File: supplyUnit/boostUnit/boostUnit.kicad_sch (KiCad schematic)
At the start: 22 parts, among them J1 Conn_02x03_Counter_Clockwise, J2 Conn_02x03_Counter_Clockwise

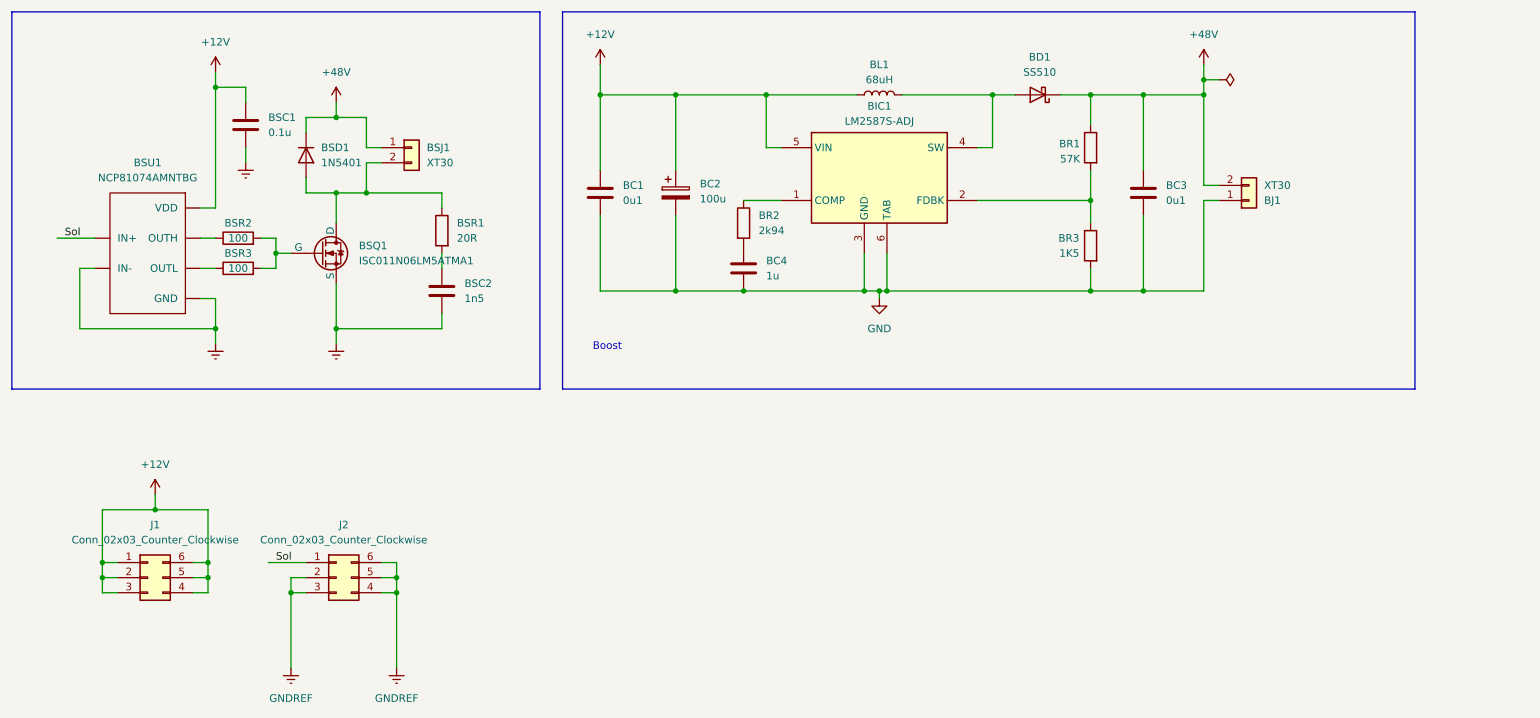
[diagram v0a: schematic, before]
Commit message: new boost
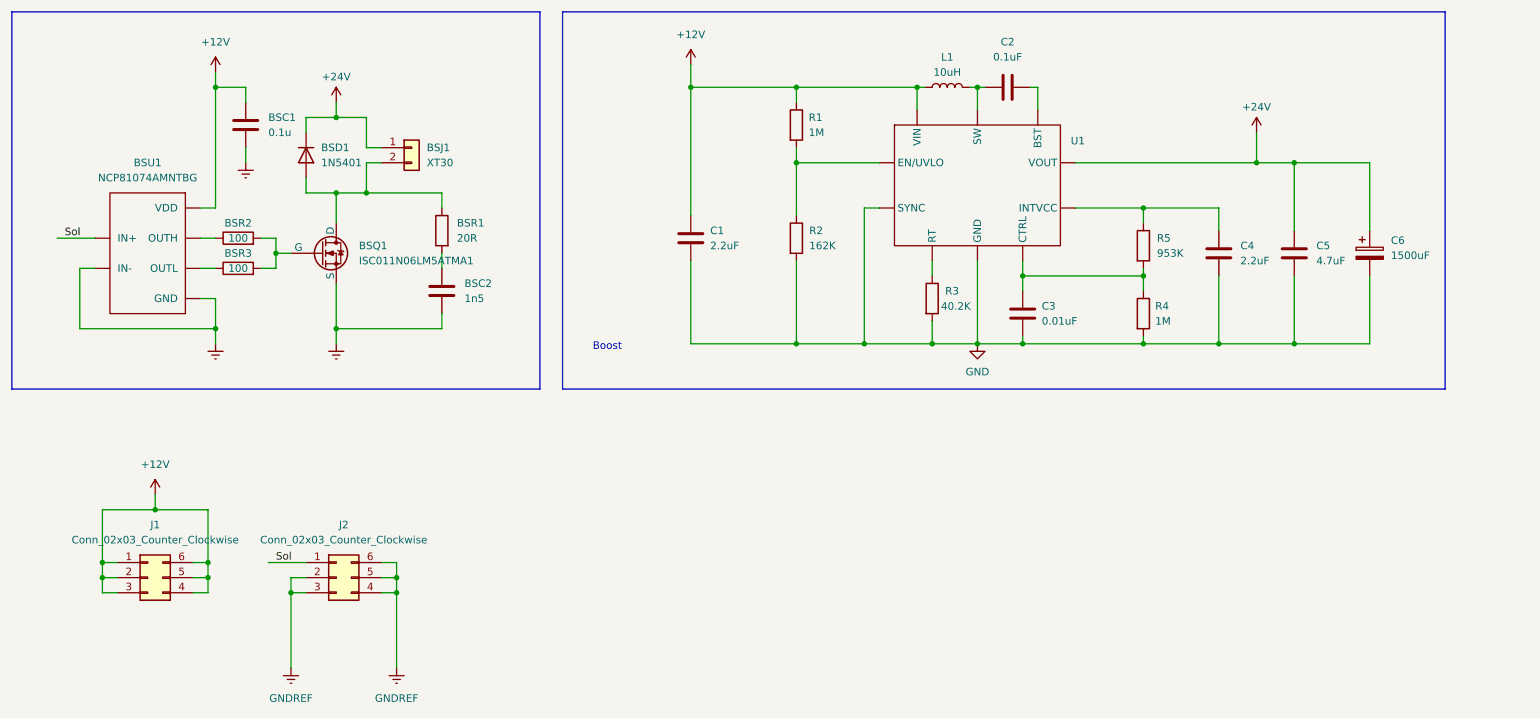
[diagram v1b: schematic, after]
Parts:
- removed BC1, BC3: 0u1, Library:cap0603, symbol Device:C
- removed BC2: 100u, Capacitor_SMD:CP_Elec_8x6.5, symbol Device:C_Polarized
- removed BC4: 1u, Library:cap0603, symbol Device:C
- removed BD1: SS510, Library:SMA (DO-214AC), symbol Device:D_Schottky
- removed BIC1: LM2587S-ADJ, Library:TO170P1435X465-6N, symbol LM2587S-ADJ_NOPB:LM2587S-ADJ_NOPB
- removed BJ1: XT30, Library:AMASS_XT30PW-F_1x02_P2.50mm_Horizontal, symbol Connector_Generic:Conn_01x02
- removed BL1: 68uH, Library:1040 One Piece Inductor, symbol Device:L
- removed BR1: 57K, Library:res0603, symbol Device:R
- removed BR2: 2k94, Library:res0603, symbol Device:R
- removed BR3: 1K5, Library:res0603, symbol Device:R
- added C1, C4: 2.2uF, Boost:cap0805, symbol Device:C
- added C2: 0.1uF, Boost:cap0402, symbol Device:C
- added C3: 0.01uF, Boost:cap0402, symbol Device:C
- added C5: 4.7uF, Boost:res0805, symbol Device:C
- added C6: 1500uF, symbol Device:C_Polarized
- added L1: 10uH, Boost:res0805, symbol Device:L
- added R1, R4: 1M, Boost:res0402, symbol Device:R
- added R2: 162K, Boost:res0402, symbol Device:R
- added R3: 40.2K, Boost:res0402, symbol Device:R
- added R5: 953K, Boost:res0402, symbol Device:R
- added U1: ~, Boost:LT8338, symbol boostUnit:LT8338
- BSC1, BSR1, BSR2, BSR3: footprint Library:res0603 -> Boost:res0603
- BSC2: footprint Library:cap0603 -> Boost:cap0603
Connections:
- net +12V: now also C1.1, L1.1, R1.1, U1.1 (VIN)
- net GND: now also C1.2, C3.2, C4.2, C5.2, C6.2, R2.2, R3.2, R4.2, U1.11 (GND), U1.6 (SYNC)
- net +48V renamed +24V
- net +24V: now also C5.1, C6.1, U1.5 (VOUT)
- new net: C3.1, R4.1, R5.2, U1.9 (CTRL)
- new net: C4.1, R5.1, U1.10 (INTVCC)
- new net: C2.2, U1.2 (BST)
- new net: R3.1, U1.7 (RT)
- new net: R1.2, R2.1, U1.8 (EN/UVLO)
- new net SW: C2.1, L1.2, U1.3 (SW), U1.4 (SW)

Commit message: boost routing
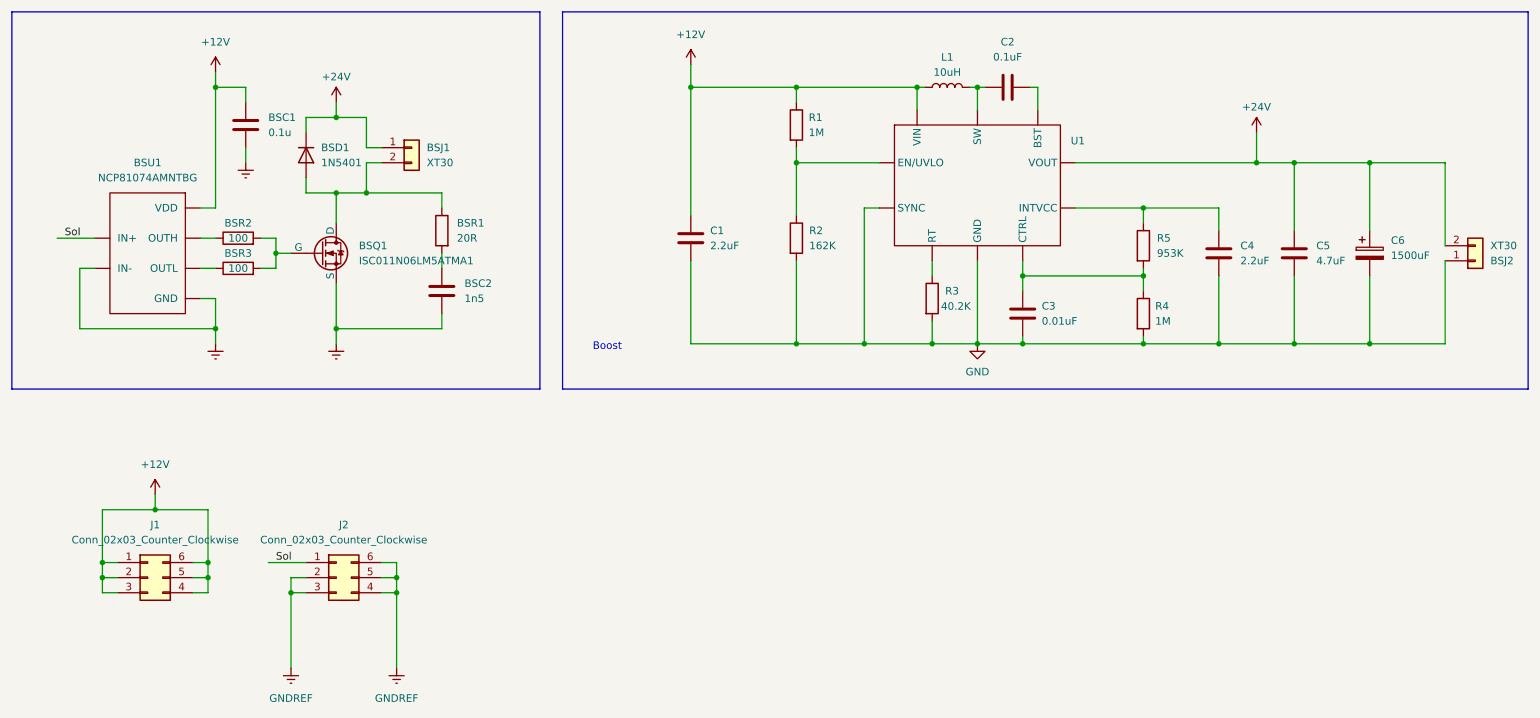
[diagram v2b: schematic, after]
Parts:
- added BSJ2: XT30, Library:AMASS_XT30PW-F_1x02_P2.50mm_Horizontal, symbol Connector_Generic:Conn_01x02
- C6: footprint (none) -> Boost:CP_Radial_D16.0mm_P7.50mm
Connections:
- net +24V: now also BSJ2.2 (Pin_2)
- net GND: now also BSJ2.1 (Pin_1)
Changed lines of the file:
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@@
+	)
+	(junction
+		(at 254 81.28)
+		(diameter 0)
+		(color 0 0 0 0)
 	)
 	(junction
@@
 	)
 	(junction
+		(at 254 50.8)
+		(diameter 0)
+		(color 0 0 0 0)
+	)
+	(junction
 		(at 241.3 81.28)
 		(diameter 0)
@@
 	(wire
 		(pts
+			(xy 266.7 67.31) (xy 266.7 81.28)
+		)
+		(stroke
+			(width 0)
+			(type default)
+		)
+	)
+	(wire
+		(pts
 			(xy 87.63 123.19) (xy 90.17 123.19)
 		)
@@
 	(wire
 		(pts
+			(xy 266.7 50.8) (xy 266.7 64.77)
+		)
+		(stroke
+			(width 0)
+			(type default)
+		)
+	)
+	(wire
+		(pts
 			(xy 33.02 63.5) (xy 39.37 63.5)
 		)
@@
 	(wire
 		(pts
+			(xy 254 50.8) (xy 266.7 50.8)
+		)
+		(stroke
+			(width 0)
+			(type default)
+		)
+	)
+	(wire
+		(pts
 			(xy 87.63 118.11) (xy 90.17 118.11)
 		)
@@
 		(pts
 			(xy 195.58 81.28) (xy 215.9 81.28)
+		)
+		(stroke
+			(width 0)
+			(type default)
+		)
+	)
+	(wire
+		(pts
+			(xy 266.7 81.28) (xy 254 81.28)
 		)
 		(stroke
@@
 	(rectangle
 		(start 118.11 25.4)
-		(end 266.7 88.9)
+		(end 280.67 88.9)
 		(stroke
 			(width 0)
@@
 			)
 		)
-		(property "Footprint" ""
+		(property "Footprint" "Boost:CP_Radial_D16.0mm_P7.50mm"
 			(at 254.9652 69.85 0)
 			(effects
@@
 					(unit 1)
 				)
+			)
+		)
+	)
+	(symbol
+		(lib_id "Connector_Generic:Conn_01x02")
+		(at 271.78 67.31 0)
+		(mirror x)
+		(unit 1)
+		(exclude_from_sim no)
+		(in_bom yes)
+		(on_board yes)
+		(dnp no)
+		(property "Reference" "BSJ2"
+			(at 274.32 67.31 0)
+			(effects
+				(font
+					(size 1.27 1.27)
+				)
+				(justify left)
+			)
+		)
+		(property "Value" "XT30"
+			(at 274.32 64.77 0)
+			(effects
+				(font
+					(size 1.27 1.27)
+				)
+				(justify left)
+			)
+		)
+		(property "Footprint" "Library:AMASS_XT30PW-F_1x02_P2.50mm_Horizontal"
+			(at 271.78 67.31 0)
+			(effects
+				(font
+					(size 1.27 1.27)
+				)
+				(hide yes)
+			)
+		)
+		(property "Datasheet" "~"
+			(at 271.78 67.31 0)
+			(effects
+				(font
+					(size 1.27 1.27)
+				)
+				(hide yes)
+			)
+		)
+		(property "Description" ""
+			(at 271.78 67.31 0)
+			(effects
+				(font
+					(size 1.27 1.27)
+				)
+				(hide yes)
+			)
+		)
+		(property "LCSC" "C108769"
+			(at 271.78 67.31 0)
+			(effects
+				(font
+					(size 1.27 1.27)
+				)
+				(hide yes)
+			)
+		)
+		(pin "1"
+		)
+		(pin "2"
+		)
+		(instances
+			(project "boostUnit"
+				(path "/697a38d4-3409-462e-879c-d6eee2cce560"
+					(reference "BSJ2")
+					(unit 1)
+				)

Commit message: Revert
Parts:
- removed BSJ2: XT30, Library:AMASS_XT30PW-F_1x02_P2.50mm_Horizontal, symbol Connector_Generic:Conn_01x02
- removed C1, C4: 2.2uF, Boost:cap0805, symbol Device:C
- removed C2: 0.1uF, Boost:cap0402, symbol Device:C
- removed C3: 0.01uF, Boost:cap0402, symbol Device:C
- removed C5: 4.7uF, Boost:res0805, symbol Device:C
- removed C6: 1500uF, Boost:CP_Radial_D16.0mm_P7.50mm, symbol Device:C_Polarized
- removed L1: 10uH, Boost:res0805, symbol Device:L
- removed R1, R4: 1M, Boost:res0402, symbol Device:R
- removed R2: 162K, Boost:res0402, symbol Device:R
- removed R3: 40.2K, Boost:res0402, symbol Device:R
- removed R5: 953K, Boost:res0402, symbol Device:R
- removed U1: ~, Boost:LT8338, symbol boostUnit:LT8338
- added BC1, BC3: 0u1, Library:cap0603, symbol Device:C
- added BC2: 100u, Capacitor_SMD:CP_Elec_8x6.5, symbol Device:C_Polarized
- added BC4: 1u, Library:cap0603, symbol Device:C
- added BD1: SS510, Library:SMA (DO-214AC), symbol Device:D_Schottky
- added BIC1: LM2587S-ADJ, Library:TO170P1435X465-6N, symbol LM2587S-ADJ_NOPB:LM2587S-ADJ_NOPB
- added BJ1: XT30, Library:AMASS_XT30PW-F_1x02_P2.50mm_Horizontal, symbol Connector_Generic:Conn_01x02
- added BL1: 68uH, Library:1040 One Piece Inductor, symbol Device:L
- added BR1: 57K, Library:res0603, symbol Device:R
- added BR2: 2k94, Library:res0603, symbol Device:R
- added BR3: 1K5, Library:res0603, symbol Device:R
- BSC1, BSR1, BSR2, BSR3: footprint Boost:res0603 -> Library:res0603
- BSC2: footprint Boost:cap0603 -> Library:cap0603
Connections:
- net +12V: now also BC1.1, BC2.1, BIC1.5 (VIN), BL1.1
- net GND: now also BC1.2, BC2.2, BC3.2, BC4.2, BIC1.3 (GND), BIC1.6 (TAB), BJ1.1 (Pin_1), BR3.2
- net +24V renamed +48V
- net +48V: now also BC3.1, BD1.1 (K), BJ1.2 (Pin_2), BR1.1
- new net: BIC1.1 (COMP), BR2.1
- new net: BIC1.2 (FDBK), BR1.2, BR3.1
- new net: BD1.2 (A), BIC1.4 (SW), BL1.2
- new net: BC4.1, BR2.2
